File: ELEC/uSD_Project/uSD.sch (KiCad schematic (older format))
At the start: 16 parts, among them J1 CONN_01X08, J2 CONN_01X08, J3 CONN_02X05, J4 CONN_01X08, J5 CONN_01X08, J6 CONN_01X01, J7 CONN_01X20, J8 CONN_01X01, U1 MCP23S17, U3 PADI_IoT_Stamp

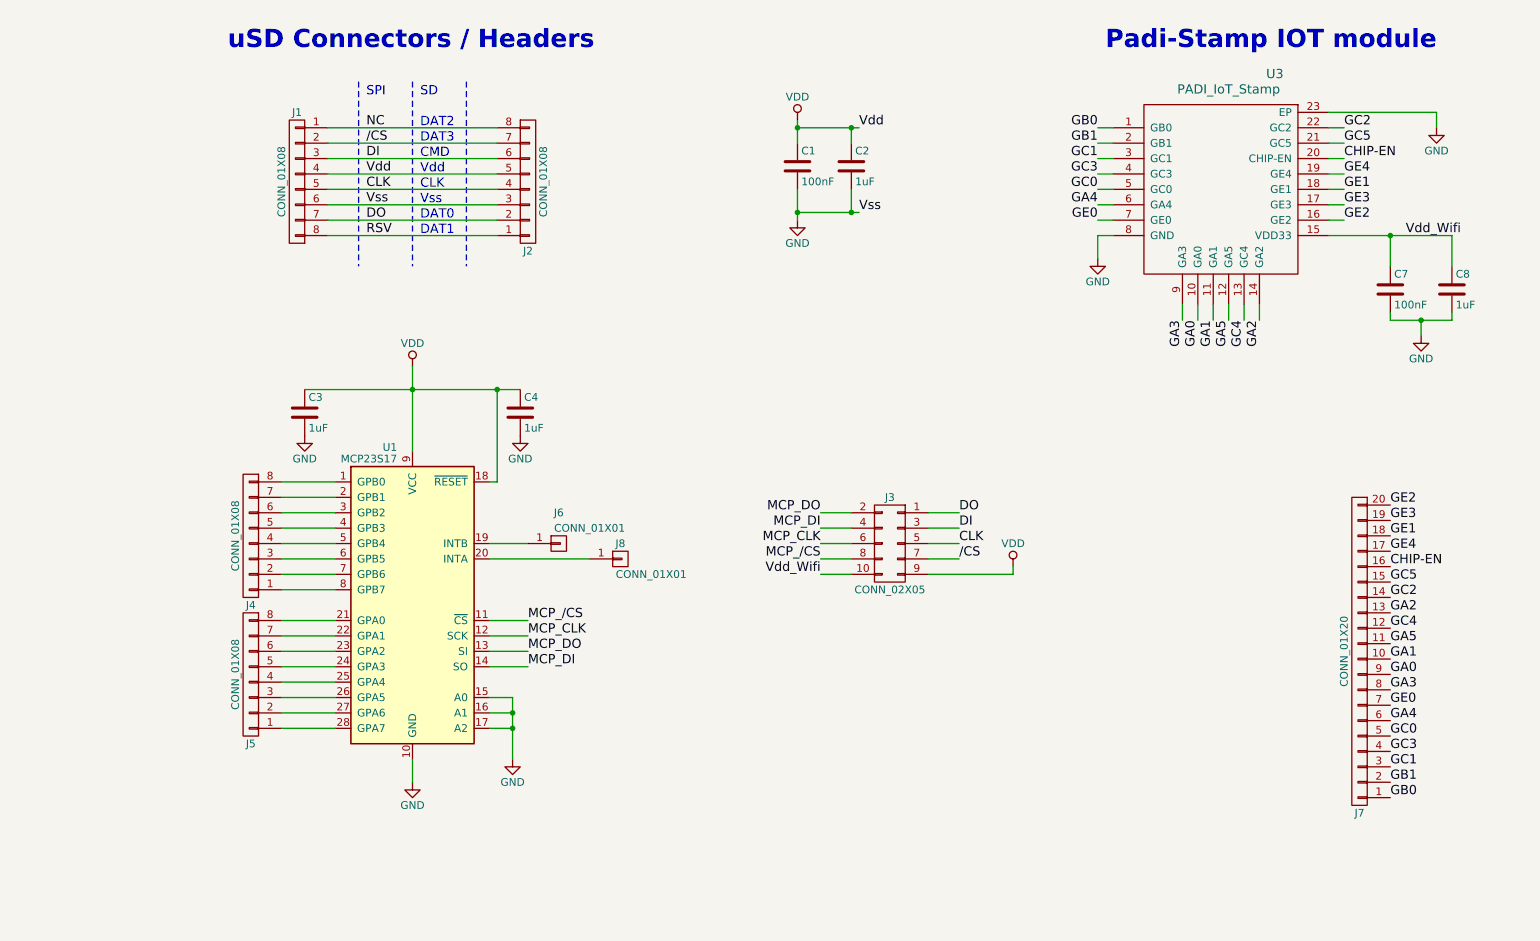
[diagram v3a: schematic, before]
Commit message: Finished layout, all the uSD pins are backwards. Last ECO
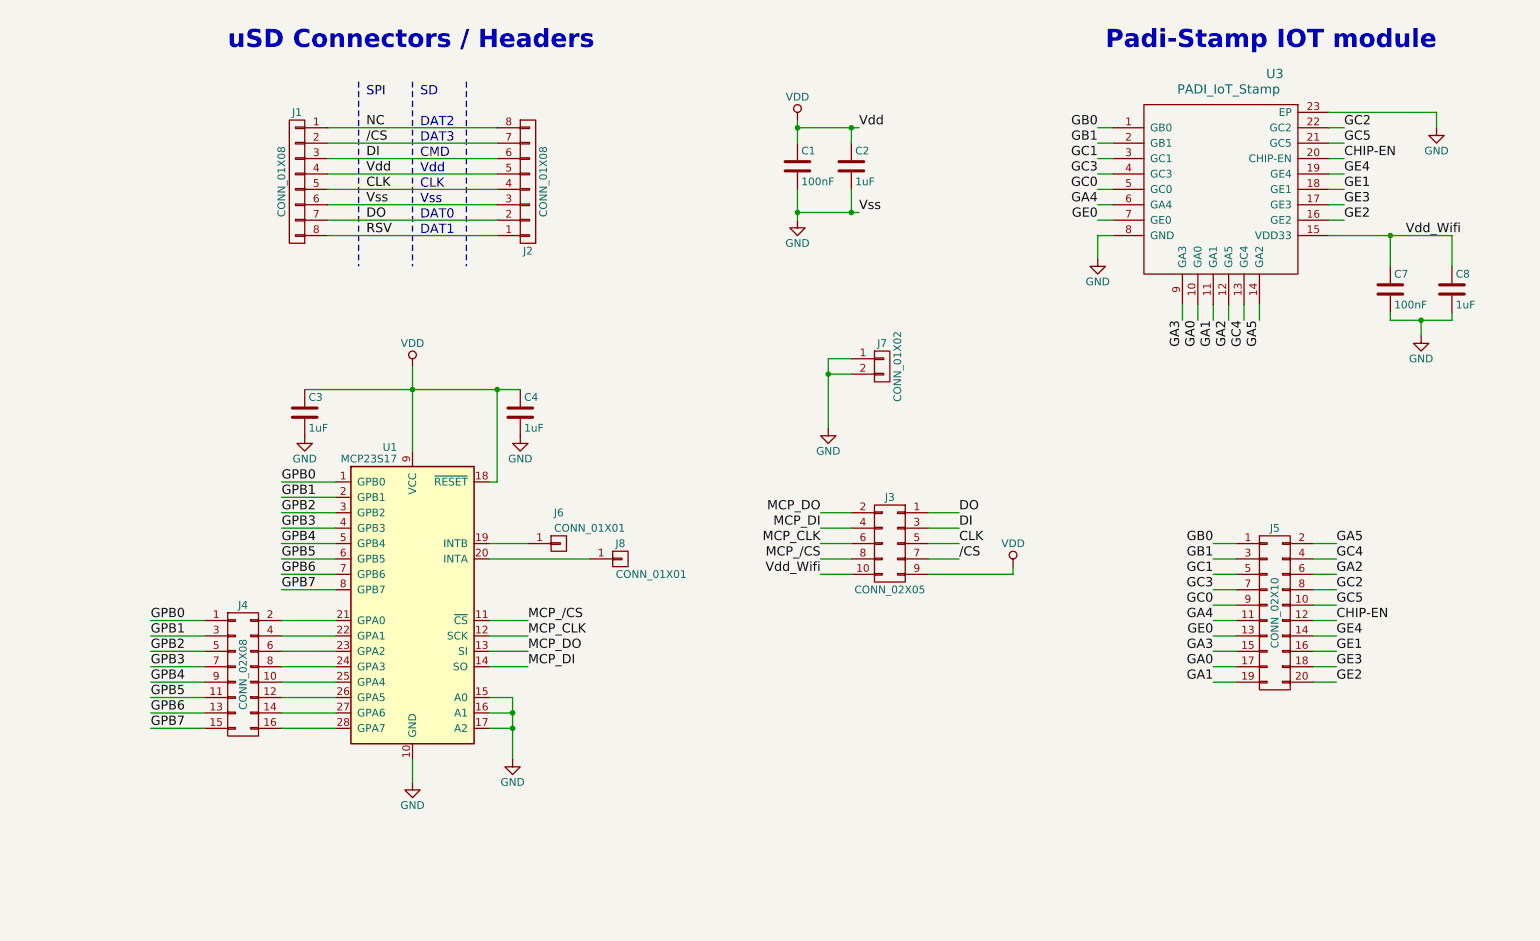
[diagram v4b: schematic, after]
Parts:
- removed J4, J5: CONN_01X08, Pin_Headers:Pin_Header_Angled_1x08_Pitch1.27mm, symbol CONN_01X08
- removed J7: CONN_01X20, Pin_Headers:Pin_Header_Angled_1x20_Pitch1.27mm, symbol CONN_01X20
- added J4: CONN_02X08, Pin_Headers:Pin_Header_Angled_2x08_Pitch2.54mm, symbol CONN_02X08
- added J5: CONN_02X10, Pin_Headers:Pin_Header_Angled_2x10_Pitch2.54mm, symbol CONN_02X10
- added J7: CONN_01X02, Pin_Headers:Pin_Header_Straight_1x02_Pitch2.54mm, symbol CONN_01X02
- J1: footprint Pin_Headers:Pin_Header_Straight_1x08_Pitch1.27mm -> Pin_Headers:Pin_Header_Straight_1x08_Pitch2.54mm
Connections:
- net CHIP-EN: now also J5.12 (P12)
- net GA0: now also J5.17 (P17)
- net GA1: now also J5.19 (P19)
- net GA2: now also U3.12 (GA5), J5.6 (P6); no longer U3.14 (GA2)
- net GA3: now also J5.15 (P15)
- net GA4: now also J5.11 (P11)
- net GA5: now also U3.14 (GA2), J5.2 (P2); no longer U3.12 (GA5)
- net GB0: now also J5.1 (P1)
- net GB1: now also J5.3 (P3)
- net GC0: now also J5.9 (P9)
- net GC1: now also J5.5 (P5)
- net GC2: now also J5.8 (P8)
- net GC3: now also J5.7 (P7)
- net GC4: now also J5.4 (P4)
- net GC5: now also J5.10 (P10)
- net GE0: now also J5.13 (P13)
- net GE1: now also J5.16 (P16)
- net GE2: now also J5.20 (P20)
- net GE3: now also J5.18 (P18)
- net GE4: now also J5.14 (P14)
- net GND: now also J7.1 (P1), J7.2 (P2)
- net GPB0: now reaches U1.1 (GPB0)
- net GPB0: now also J4.1 (P1)
- net GPB1: now reaches U1.2 (GPB1)
- net GPB1: now also J4.3 (P3)
- net at U1.21 (GPA0): now also J4.2 (P2)
- net at U1.22 (GPA1): now also J4.4 (P4)
- net at U1.23 (GPA2): now also J4.6 (P6)
- net at U1.24 (GPA3): now also J4.8 (P8)
- net at U1.25 (GPA4): now also J4.10 (P10)
- net at U1.26 (GPA5): now also J4.12 (P12)
- net at U1.27 (GPA6): now also J4.14 (P14)
- net at U1.28 (GPA7): now also J4.16 (P16)
- net GPB2: now reaches U1.3 (GPB2)
- net GPB2: now also J4.5 (P5)
- net GPB3: now reaches U1.4 (GPB3)
- net GPB3: now also J4.7 (P7)
- net GPB4: now reaches U1.5 (GPB4)
- net GPB4: now also J4.9 (P9)
- net GPB5: now reaches U1.6 (GPB5)
- net GPB5: now also J4.11 (P11)
- net GPB6: now reaches U1.7 (GPB6)
- net GPB6: now also J4.13 (P13)
- net GPB7: now reaches U1.8 (GPB7)
- net GPB7: now also J4.15 (P15)
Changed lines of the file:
@@
 F 0 "J1" H 2800 2300 50  0000 C CNN
 F 1 "CONN_01X08" V 2900 1850 50  0000 C CNN
-F 2 "Pin_Headers:Pin_Header_Straight_1x08_Pitch1.27mm" H 2800 1850 50  0001 C CNN
+F 2 "Pin_Headers:Pin_Header_Straight_1x08_Pitch2.54mm" H 2800 1850 50  0001 C CNN
 F 3 "" H 2800 1850 50  0001 C CNN
 	1    2800 1850
@@
 Text Label 8750 2750 3    60   ~ 0
 GA1
-Text Label 8850 2750 3    60   ~ 0
+Text Label 9050 2750 3    60   ~ 0
 GA5
 Text Label 8950 2750 3    60   ~ 0
 GC4
-Text Label 9050 2750 3    60   ~ 0
+Text Label 8850 2750 3    60   ~ 0
 GA2
 Text Label 9600 1700 0    60   ~ 0
@@
 Text Label 9600 2100 0    60   ~ 0
 GE2
-Text Label 9900 4350 0    60   ~ 0
+Text Label 9550 4700 0    60   ~ 0
 CHIP-EN
-Text Label 9900 4250 0    60   ~ 0
+Text Label 9550 4800 0    60   ~ 0
 GE4
-Text Label 9900 4550 0    60   ~ 0
+Text Label 9550 4500 0    60   ~ 0
 GC2
-Text Label 9900 4450 0    60   ~ 0
+Text Label 9550 4600 0    60   ~ 0
 GC5
-Text Label 9900 4150 0    60   ~ 0
+Text Label 9550 4900 0    60   ~ 0
 GE1
-Text Label 9900 4050 0    60   ~ 0
+Text Label 9550 5000 0    60   ~ 0
 GE3
-Text Label 9900 3950 0    60   ~ 0
+Text Label 9550 5100 0    60   ~ 0
 GE2
-Text Label 9900 5150 0    60   ~ 0
+Text Label 8750 4900 2    60   ~ 0
 GA3
-Text Label 9900 5050 0    60   ~ 0
+Text Label 8750 5000 2    60   ~ 0
 GA0
-Text Label 9900 4950 0    60   ~ 0
+Text Label 8750 5100 2    60   ~ 0
 GA1
-Text Label 9900 4850 0    60   ~ 0
+Text Label 9550 4200 0    60   ~ 0
 GA5
-Text Label 9900 4750 0    60   ~ 0
+Text Label 9550 4300 0    60   ~ 0
 GC4
-Text Label 9900 4650 0    60   ~ 0
+Text Label 9550 4400 0    60   ~ 0
 GA2
-Text Label 9900 5850 0    60   ~ 0
+Text Label 8750 4200 2    60   ~ 0
 GB0
-Text Label 9900 5750 0    60   ~ 0
+Text Label 8750 4300 2    60   ~ 0
 GB1
-Text Label 9900 5650 0    60   ~ 0
+Text Label 8750 4400 2    60   ~ 0
 GC1
-Text Label 9900 5550 0    60   ~ 0
+Text Label 8750 4500 2    60   ~ 0
 GC3
-Text Label 9900 5450 0    60   ~ 0
+Text Label 8750 4600 2    60   ~ 0
 GC0
-Text Label 9900 5350 0    60   ~ 0
+Text Label 8750 4700 2    60   ~ 0
 GA4
-Text Label 9900 5250 0    60   ~ 0
+Text Label 8750 4800 2    60   ~ 0
 GE0
-$Comp
-L CONN_01X20 J7
-U 1 1 59AFB59F
-P 9700 4900
-F 0 "J7" H 9700 5950 50  0000 C CNN
-F 1 "CONN_01X20" V 9800 4900 50  0000 C CNN
-F 2 "Pin_Headers:Pin_Header_Angled_1x20_Pitch1.27mm" H 9700 4900 50  0001 C CNN
-F 3 "" H 9700 4900 50  0001 C CNN
-	1    9700 4900
-	-1   0    0    1
-$EndComp
 $Comp
 L MCP23S17 U1
@@
 Connection ~ 4100 3200
 $Comp
-L CONN_01X08 J4
-U 1 1 59B0C30D
-P 2500 4150
-F 0 "J4" H 2500 4600 50  0000 C CNN
-F 1 "CONN_01X08" V 2600 4150 50  0000 C CNN
-F 2 "Pin_Headers:Pin_Header_Angled_1x08_Pitch1.27mm" H 2500 4150 50  0001 C CNN
-F 3 "" H 2500 4150 50  0001 C CNN
-	1    2500 4150
-	-1   0    0    1
-$EndComp
-$Comp
-L CONN_01X08 J5
-U 1 1 59B0C44B
-P 2500 5050
-F 0 "J5" H 2500 5500 50  0000 C CNN
-F 1 "CONN_01X08" V 2600 5050 50  0000 C CNN
-F 2 "Pin_Headers:Pin_Header_Angled_1x08_Pitch1.27mm" H 2500 5050 50  0001 C CNN
-F 3 "" H 2500 5050 50  0001 C CNN
-	1    2500 5050
-	-1   0    0    1
-$EndComp
-$Comp
 L C C3
 U 1 1 59B0D238
@@
 Text Label 6200 4400 2    60   ~ 0
 Vdd_Wifi
+$Comp
+L CONN_02X10 J5
+U 1 1 59B32A70
+P 9150 4650
+F 0 "J5" H 9150 5200 50  0000 C CNN
+F 1 "CONN_02X10" V 9150 4650 50  0000 C CNN
+F 2 "Pin_Headers:Pin_Header_Angled_2x10_Pitch2.54mm" H 9150 3450 50  0001 C CNN
+F 3 "" H 9150 3450 50  0001 C CNN
+	1    9150 4650
+	1    0    0    -1
+$EndComp
+$Comp
+L CONN_02X08 J4
+U 1 1 59B32DE5
+P 2450 5050
+F 0 "J4" H 2450 5500 50  0000 C CNN
+F 1 "CONN_02X08" V 2450 5050 50  0000 C CNN
+F 2 "Pin_Headers:Pin_Header_Angled_2x08_Pitch2.54mm" H 2450 3850 50  0001 C CNN
+F 3 "" H 2450 3850 50  0001 C CNN
+	1    2450 5050
+	1    0    0    -1
+$EndComp
+Text Label 2700 3800 0    60   ~ 0
+GPB0
+Text Label 2700 3900 0    60   ~ 0
+GPB1
+Text Label 2700 4000 0    60   ~ 0
+GPB2
+Text Label 2700 4100 0    60   ~ 0
+GPB3
+Text Label 2700 4200 0    60   ~ 0
+GPB4
+Text Label 2700 4300 0    60   ~ 0
+GPB5
+Text Label 2700 4400 0    60   ~ 0
+GPB6
+Text Label 2700 4500 0    60   ~ 0
+GPB7
+Wire Wire Line
+	2200 4700 1850 4700
+Wire Wire Line
+	1850 4800 2200 4800
+Wire Wire Line
+	2200 5100 1850 5100
+Wire Wire Line
+	1850 5000 2200 5000
+Wire Wire Line
+	2200 4900 1850 4900
+Wire Wire Line
+	2200 5400 1850 5400
+Wire Wire Line
+	1850 5300 2200 5300
+Wire Wire Line
+	2200 5200 1850 5200
+Text Label 1850 4700 0    60   ~ 0
+GPB0
+Text Label 1850 4800 0    60   ~ 0
+GPB1
+Text Label 1850 4900 0    60   ~ 0
+GPB2
+Text Label 1850 5000 0    60   ~ 0
+GPB3
+Text Label 1850 5100 0    60   ~ 0
+GPB4
+Text Label 1850 5200 0    60   ~ 0
+GPB5
+Text Label 1850 5300 0    60   ~ 0
+GPB6
+Text Label 1850 5400 0    60   ~ 0
+GPB7
+Wire Wire Line
+	8900 5100 8750 5100
+Wire Wire Line
+	8900 5000 8750 5000
+Wire Wire Line
+	8900 4900 8750 4900
+Wire Wire Line
+	8900 4800 8750 4800
+Wire Wire Line
+	8900 4700 8750 4700
+Wire Wire Line
+	8900 4600 8750 4600
+Wire Wire Line
+	8900 4500 8750 4500
+Wire Wire Line
+	8900 4400 8750 4400
+Wire Wire Line
+	8900 4300 8750 4300
+Wire Wire Line
+	8900 4200 8750 4200
+Wire Wire Line
+	9550 5100 9400 5100
+Wire Wire Line
+	9550 5000 9400 5000
+Wire Wire Line
+	9550 4900 9400 4900
+Wire Wire Line
+	9550 4800 9400 4800
+Wire Wire Line
+	9550 4700 9400 4700
+Wire Wire Line
+	9550 4600 9400 4600
+Wire Wire Line
+	9550 4500 9400 4500
+Wire Wire Line
+	9550 4400 9400 4400
+Wire Wire Line
+	9550 4300 9400 4300
+Wire Wire Line
+	9550 4200 9400 4200
+$Comp
+L CONN_01X02 J7
+U 1 1 59B354B7
+P 6600 3050
+F 0 "J7" H 6600 3200 50  0000 C CNN
+F 1 "CONN_01X02" V 6700 3050 50  0000 C CNN
+F 2 "Pin_Headers:Pin_Header_Straight_1x02_Pitch2.54mm" H 6600 3050 50  0001 C CNN
+F 3 "" H 6600 3050 50  0001 C CNN
+	1    6600 3050
+	1    0    0    -1
+$EndComp
+Wire Wire Line
+	6400 3000 6250 3000
+Wire Wire Line
+	6250 3000 6250 3450
+Wire Wire Line
+	6400 3100 6250 3100
+Connection ~ 6250 3100
+$Comp
+L GND #PWR012
+U 1 1 59B35707
+P 6250 3450
+F 0 "#PWR012" H 6250 3200 50  0001 C CNN
+F 1 "GND" H 6250 3300 50  0000 C CNN
+F 2 "" H 6250 3450 50  0001 C CNN
+F 3 "" H 6250 3450 50  0001 C CNN
+	1    6250 3450
+	1    0    0    -1
+$EndComp
 $EndSCHEMATC

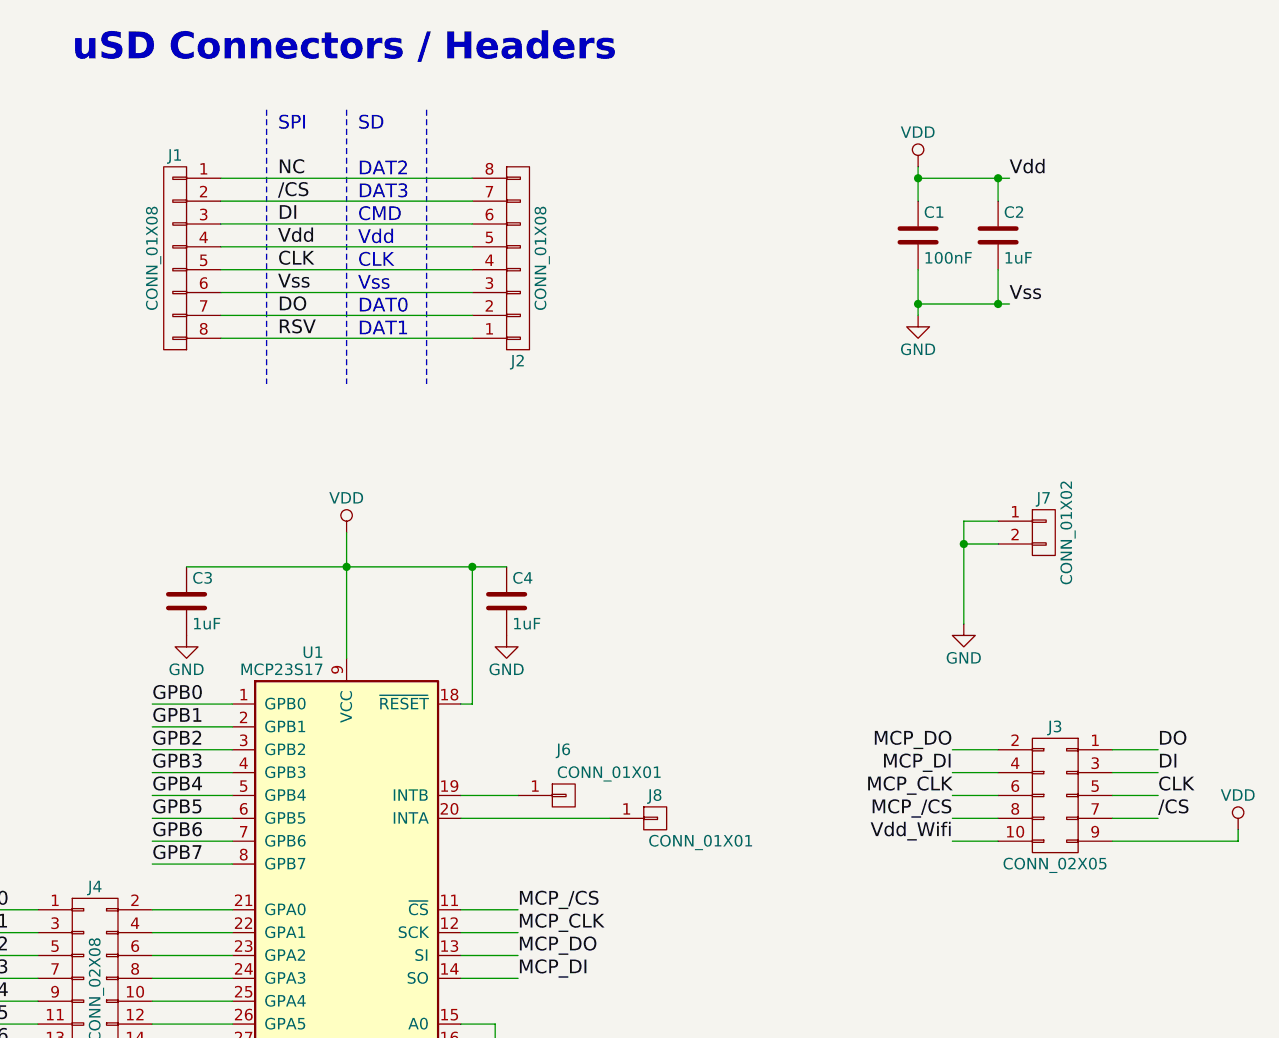
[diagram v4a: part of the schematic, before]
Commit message: Flipped uSD connector so it's proper, generated gerbers, ordered PCBs!
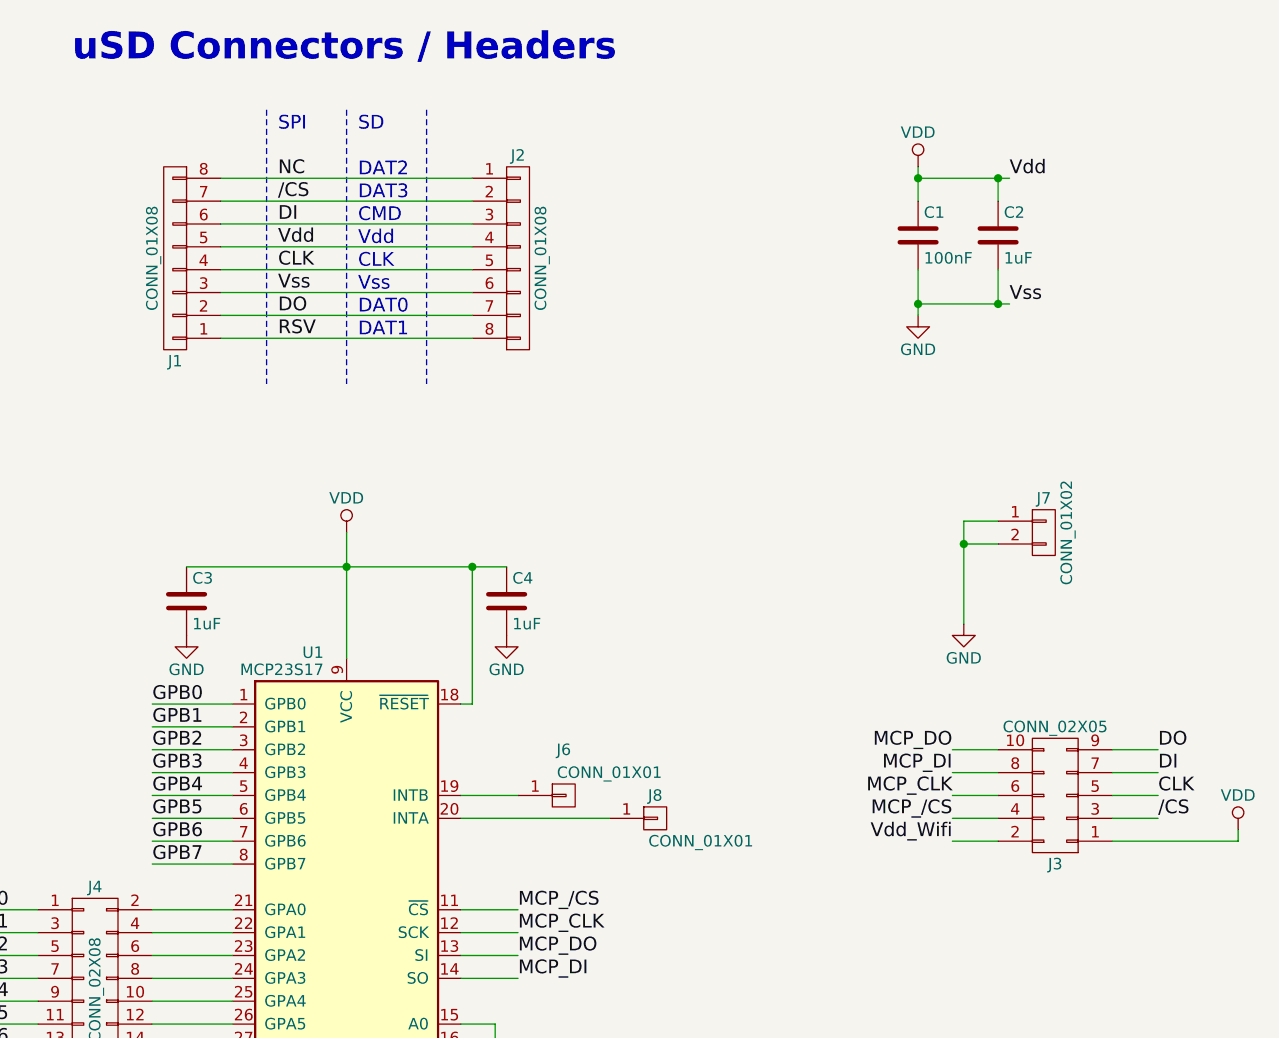
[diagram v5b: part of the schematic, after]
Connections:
- net /CS: now also J1.7 (P7), J2.2 (P2), J3.3 (P3); no longer J1.2 (P2), J2.7 (P7), J3.7 (P7)
- net CLK: now also J1.4 (P4), J2.5 (P5); no longer J1.5 (P5), J2.4 (P4)
- net DI: now also J1.6 (P6), J2.3 (P3), J3.7 (P7); no longer J1.3 (P3), J2.6 (P6), J3.3 (P3)
- net DO: now also J1.2 (P2), J2.7 (P7), J3.9 (P9); no longer J1.7 (P7), J2.2 (P2), J3.1 (P1)
- net GND: now also J1.3 (P3), J2.6 (P6); no longer J1.6 (P6), J2.3 (P3)
- net MCP_/CS: now also J3.4 (P4); no longer J3.8 (P8)
- net MCP_DI: now also J3.8 (P8); no longer J3.4 (P4)
- net MCP_DO: now also J3.10 (P10); no longer J3.2 (P2)
- net NC: now also J1.8 (P8), J2.1 (P1); no longer J1.1 (P1), J2.8 (P8)
- net RSV: now also J1.1 (P1), J2.8 (P8); no longer J1.8 (P8), J2.1 (P1)
- net VDD: now also J1.5 (P5), J2.4 (P4), J3.1 (P1); no longer J1.4 (P4), J2.5 (P5), J3.9 (P9)
- net Vdd_Wifi: now also J3.2 (P2); no longer J3.10 (P10)
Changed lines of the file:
@@
 F 3 "" H 2800 1850 50  0001 C CNN
 	1    2800 1850
-	-1   0    0    -1
+	-1   0    0    1
 $EndComp
 Wire Wire Line
@@
 F 3 "" H 4300 1850 50  0001 C CNN
 	1    4300 1850
-	1    0    0    1
+	1    0    0    -1
 $EndComp
 Text Label 7100 4000 0    60   ~ 0
@@
 F 3 "" H 6650 3000 50  0001 C CNN
 	1    6650 4200
-	-1   0    0    -1
-$EndComp
-$Comp
+	-1   0    0    1
+$EndComp
+$Comp
